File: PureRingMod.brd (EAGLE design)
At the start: 160 x 100 mm, 31 parts, among them IC1 TL074P, IC2 TL072P, X1 NC3FD-V

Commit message: latest
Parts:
- moved C1 164.3 mm to (82.5, 3.81)
- moved D2 152.6 mm to (82.5, 24.1)
- moved D1 144.9 mm to (82.5, 20.3)
- moved C5 143.5 mm to (74.9, 55.9)
- moved R5 142.3 mm to (76.2, 52.1)
- moved R11 141.5 mm to (76.2, 11.4)
- moved POWER 137.2 mm to (92.7, 15.2)
- moved R13 134.7 mm to (63.5, 52.1)
- moved IC2 133.8 mm to (63.5, 14.0)
- moved R16 128.1 mm to (83.8, 43.2)
- moved R3 126.9 mm to (76.2, 31.8)
- moved R10 125.5 mm to (63.5, 5.08)
- moved MP1 118.6 mm to (63.5, 27.9)
- moved R12 117.7 mm to (53.3, 41.9), turned to 90 degrees
- moved R15 117.4 mm to (86.4, 55.9), turned to 180 degrees
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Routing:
- net GND: track 0.00 -> 271.0 mm
- net N$27: track 0.00 -> 86.9 mm
- net N$25: track 0.00 -> 86.7 mm
- net -12V: track 0.00 -> 76.7 mm
- net N$24: track 0.00 -> 70.6 mm
- net +12V: track 0.00 -> 70.2 mm
- net N$15: track 0.00 -> 63.7 mm
- net N$4: track 0.00 -> 61.5 mm
- net N$19: track 0.00 -> 61.0 mm
- net N$1: track 0.00 -> 43.0 mm
- net N$7: track 0.00 -> 35.4 mm
- net N$12: track 0.00 -> 34.3 mm
- net N$5: track 0.00 -> 26.0 mm
- net N$22: track 0.00 -> 22.4 mm
- net N$23: track 0.00 -> 20.9 mm
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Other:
- board size 160 x 100 mm -> 99 x 60.6 mm

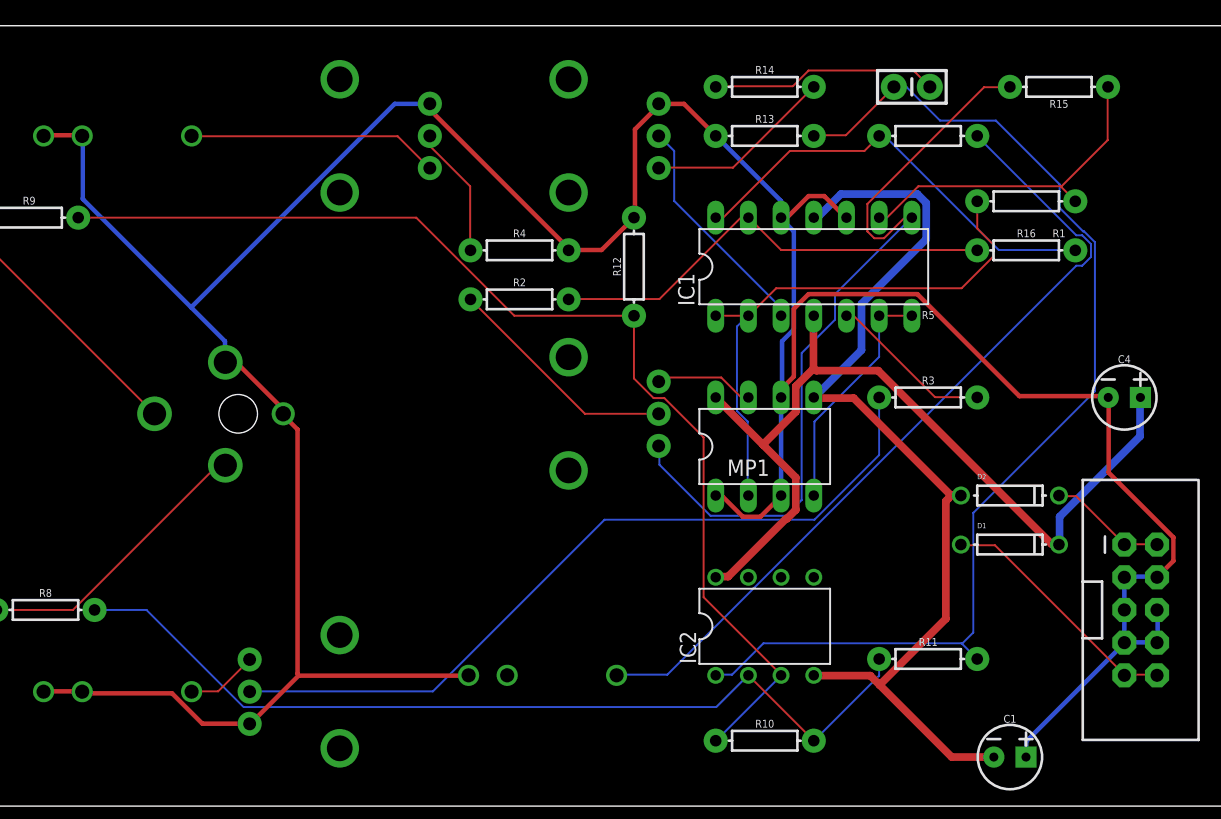
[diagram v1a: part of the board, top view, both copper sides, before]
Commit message: Fixed wiring errors
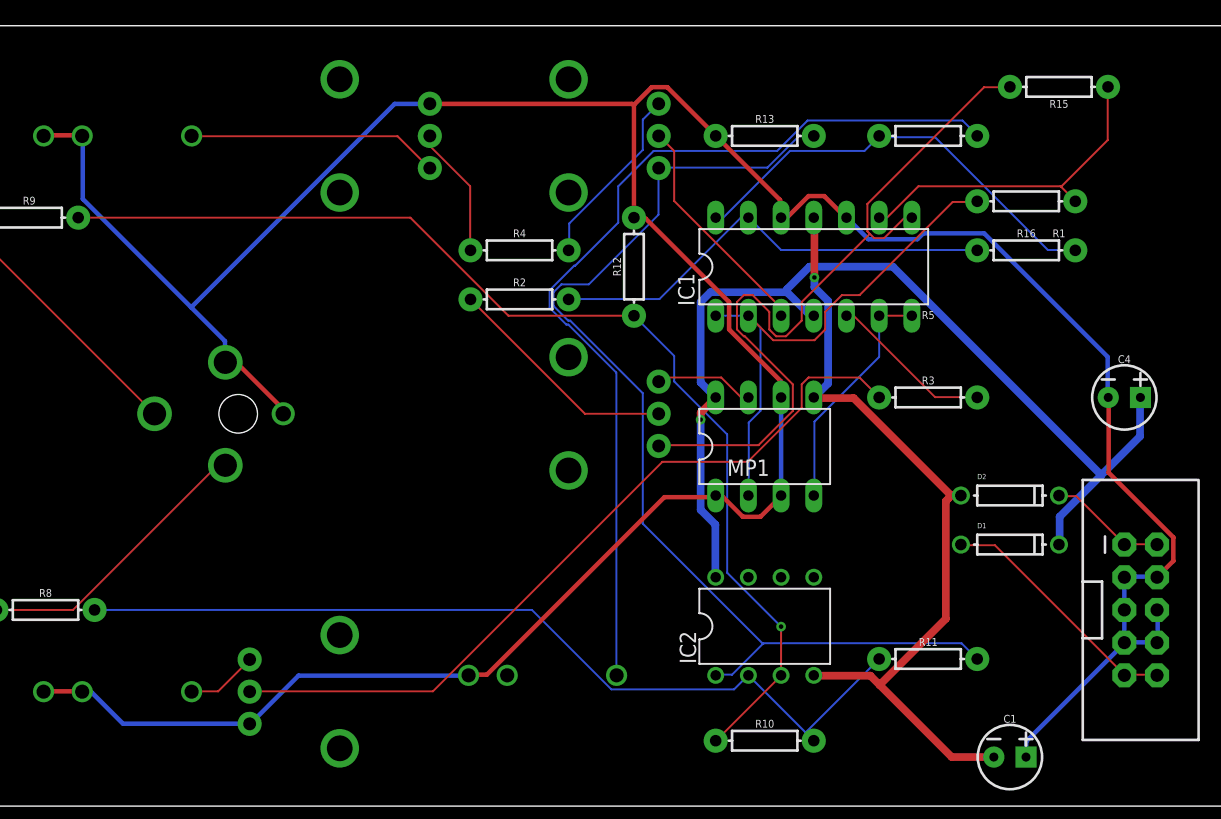
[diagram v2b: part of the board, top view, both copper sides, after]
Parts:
- removed C5: 4u7f, SparkFun-Capacitors:CAP-PTH-SMALL-KIT
- removed R14: 100, SparkFun-Resistors:AXIAL-0.3
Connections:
- removed net N$26: C5.2, R14.P$1
- removed net N$29: MICMIX.P$3, R14.P$2
- new net N$8: MICMIX.P$1, R4.P$2
- net GND: no longer MICMIX.P$1, R4.P$2
- net N$27: now also MICMIX.P$3; no longer C5.1
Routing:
- net N$26: track 17.7 -> 0.00 mm
- net N$29: track 14.7 -> 0.00 mm
- net N$8: track 0.00 -> 14.3 mm
- net -12V: track 76.7 -> 63.2 mm, vias 0 -> 1
- net N$15: track 63.7 -> 73.0 mm
- net +12V: track 70.2 -> 78.8 mm, vias 0 -> 1
- net N$27: track 86.9 -> 83.4 mm
- net GND: track 271.0 -> 268.5 mm
- net N$1: track 43.0 -> 41.2 mm
- net N$4: track 61.5 -> 60.0 mm
- net N$24: track 70.6 -> 69.1 mm
- net N$25: track 86.7 -> 86.2 mm, vias 0 -> 1

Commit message: updated board
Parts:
- moved R9 47.6 mm to (45.7, 19.1)
- moved R8 38.1 mm to (45.7, 15.2)
- moved R15 16.7 mm to (83.8, 39.4)
- moved R11 3.81 mm to (76.2, 15.2)
- moved CARRIER 3.59 mm to (11.4, 49.5)
- moved MODULATOR 2.84 mm to (11.4, 7.62)
- moved MICMIX 2.84 mm to (47.0, 49.5)
- moved MIX 2.84 mm to (47.0, 27.9)
- moved R12 2.84 mm to (54.6, 39.4)
- moved R2 2.84 mm to (45.7, 36.8)
- moved R4 2.84 mm to (45.7, 40.6)
- moved VOLCARIER 2.54 mm to (30.5, 49.5)
- moved X1 2.54 mm to (21.6, 27.9)
- moved OUTPUT 2.44 mm to (47.0, 7.72)
- moved VOLMOD 1.27 mm to (30.5, 7.62), turned to 270 degrees
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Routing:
- net N$25: track 86.2 -> 43.7 mm, vias 1 -> 0
- net N$24: track 69.1 -> 32.8 mm
- net N$17: track 5.57 -> 22.1 mm
- net N$19: track 60.7 -> 45.6 mm
- net N$23: track 20.9 -> 34.6 mm
- net N$4: track 60.0 -> 46.6 mm
- net GND: track 268.5 -> 259.8 mm
- net -12V: track 63.2 -> 67.4 mm
- net N$27: track 83.4 -> 86.8 mm
- net N$16: track 19.6 -> 22.1 mm
- net N$6: track 18.3 -> 15.8 mm
- net N$15: track 73.0 -> 75.4 mm
- net N$1: track 41.2 -> 43.5 mm
- net N$30: track 17.9 -> 16.0 mm
- net N$22: track 22.4 -> 23.9 mm
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- added copper zone on layer 16, net GND
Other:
- board size 99 x 60.6 mm -> 99 x 58.1 mm

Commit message: V1.0 board
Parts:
- added GAIN: 9MMPOT, GMSN:POT
- added OUTPUT2: Output2, INSTRUO:S_JACK
- added R6: 1K, SparkFun-Resistors:AXIAL-0.3
- added U$2: (no value), gmsnLogo:GMSN!_LOGO
- R16: value 100K -> 10K
- R2: value 20K -> 10K
- moved R13 36.9 mm to (64.8, 15.2)
- moved C1 33.7 mm to (94.0, 36.8), turned to 180 degrees
- moved R5 30.7 mm to (80.0, 21.6)
- moved MP1 24.7 mm to (49.5, 7.62)
- moved OUTPUT 19.1 mm to (66.0, 7.62)
- moved IC2 18.5 mm to (81.3, 8.89)
- moved R10 14.0 mm to (64.8, 19.1)
- moved R3 8.03 mm to (83.8, 34.3)
- moved D1 6.48 mm to (83.8, 26.7)
- moved D2 6.48 mm to (83.8, 30.5)
- moved R11 4.58 mm to (80.0, 17.8)
- moved C4 2.84 mm to (94.0, 30.5)
- moved IC1 2.54 mm to (67.3, 39.4)
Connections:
- new net N$20: OUTPUT2.TIP, R6.P$2
- new net N$5: GAIN.P$1, R16.P$1
- net GND: now also OUTPUT2.GND
- net N$12: now also R6.P$1
- net N$7: now also GAIN.P$2, GAIN.P$3; no longer R16.P$1
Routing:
- net -12V: track 67.4 -> 127.9 mm, vias 1 -> 0
- net N$15: track 75.4 -> 19.3 mm
- net N$2: track 18.6 -> 45.5 mm
- net N$12: track 34.3 -> 61.0 mm
- net N$1: track 43.5 -> 67.7 mm
- net N$25: track 43.7 -> 61.6 mm
- net N$19: track 45.6 -> 63.1 mm
- net N$5: track 0.00 -> 15.6 mm
- net +12V: track 79.5 -> 93.7 mm, vias 0 -> 1
- net N$20: track 0.00 -> 12.6 mm
- net N$3: track 9.00 -> 21.4 mm
- net N$27: track 86.8 -> 75.4 mm, vias 0 -> 1
- net N$24: track 32.8 -> 43.1 mm
- net N$11: track 12.8 -> 19.3 mm
- net GND: track 259.8 -> 266.0 mm
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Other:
- board text added: "CC BY 3.0"
- board text added: "Ring Modulator Design Andy C From a design by Roman Sowa"
- board text added: "V1.0"
